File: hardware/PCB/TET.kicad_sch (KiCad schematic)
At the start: 43 parts, among them J1 SWD, M1 MountingHole, M2 MountingHole, M3 MountingHole, M4 MountingHole, U1 TCAN330GDCNR, U2 8 MHz, U3 STM32L431RBT6TR, U4 TMP112AIDRLR

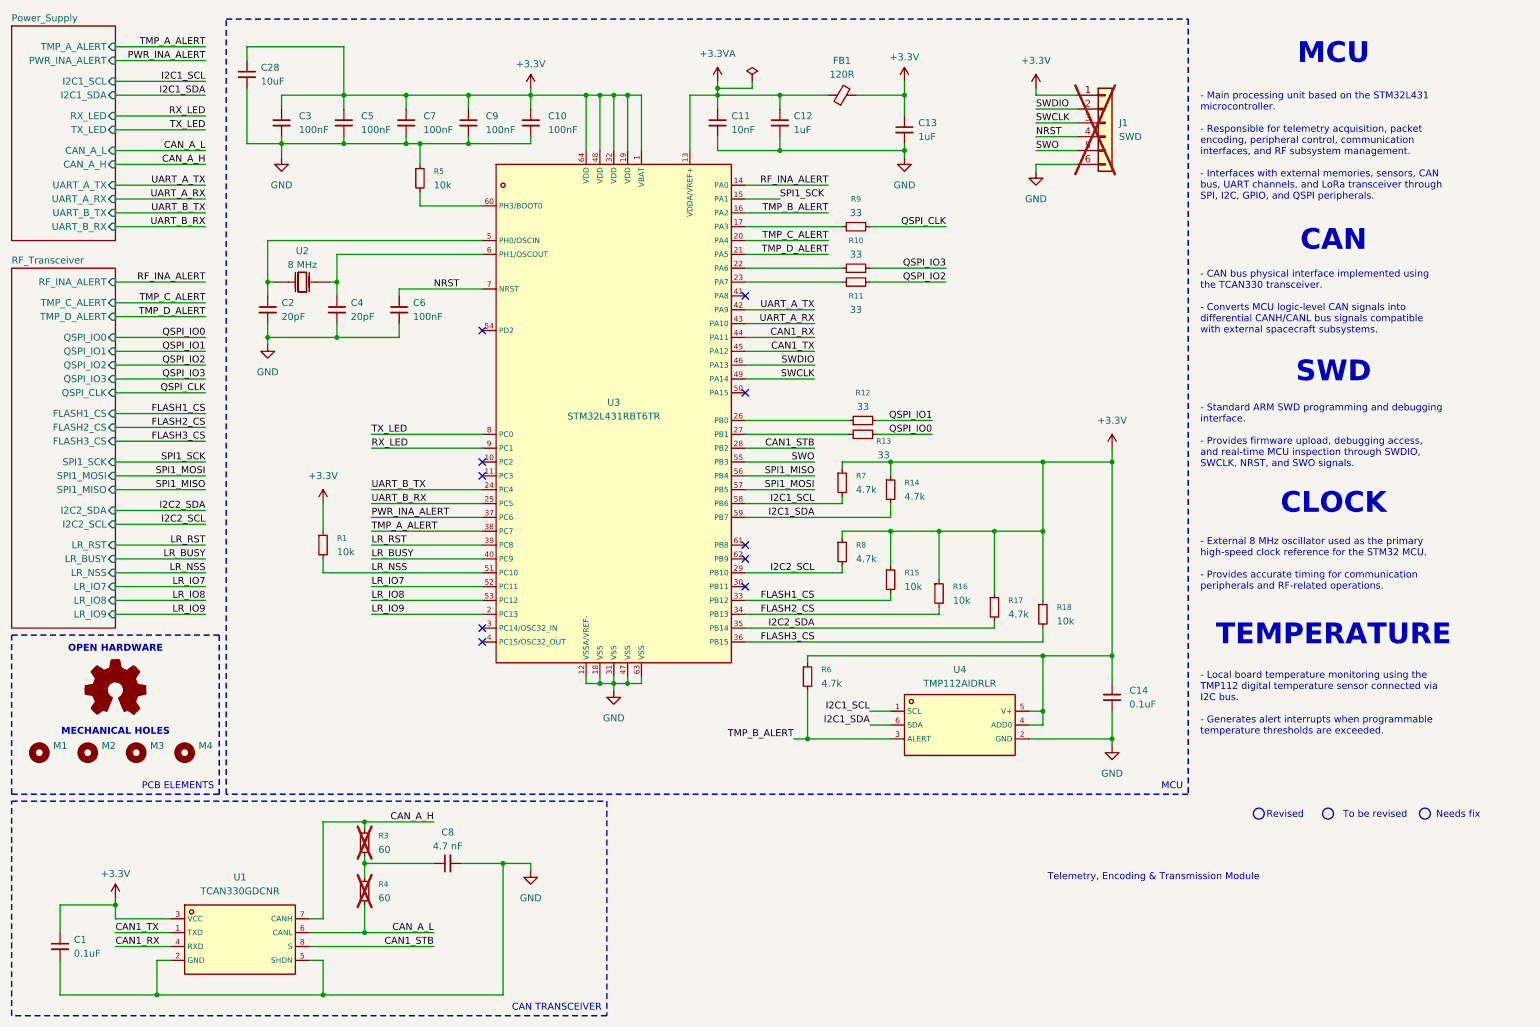
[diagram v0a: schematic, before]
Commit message: feat(hardware): implement TET module PCB design and restructure project
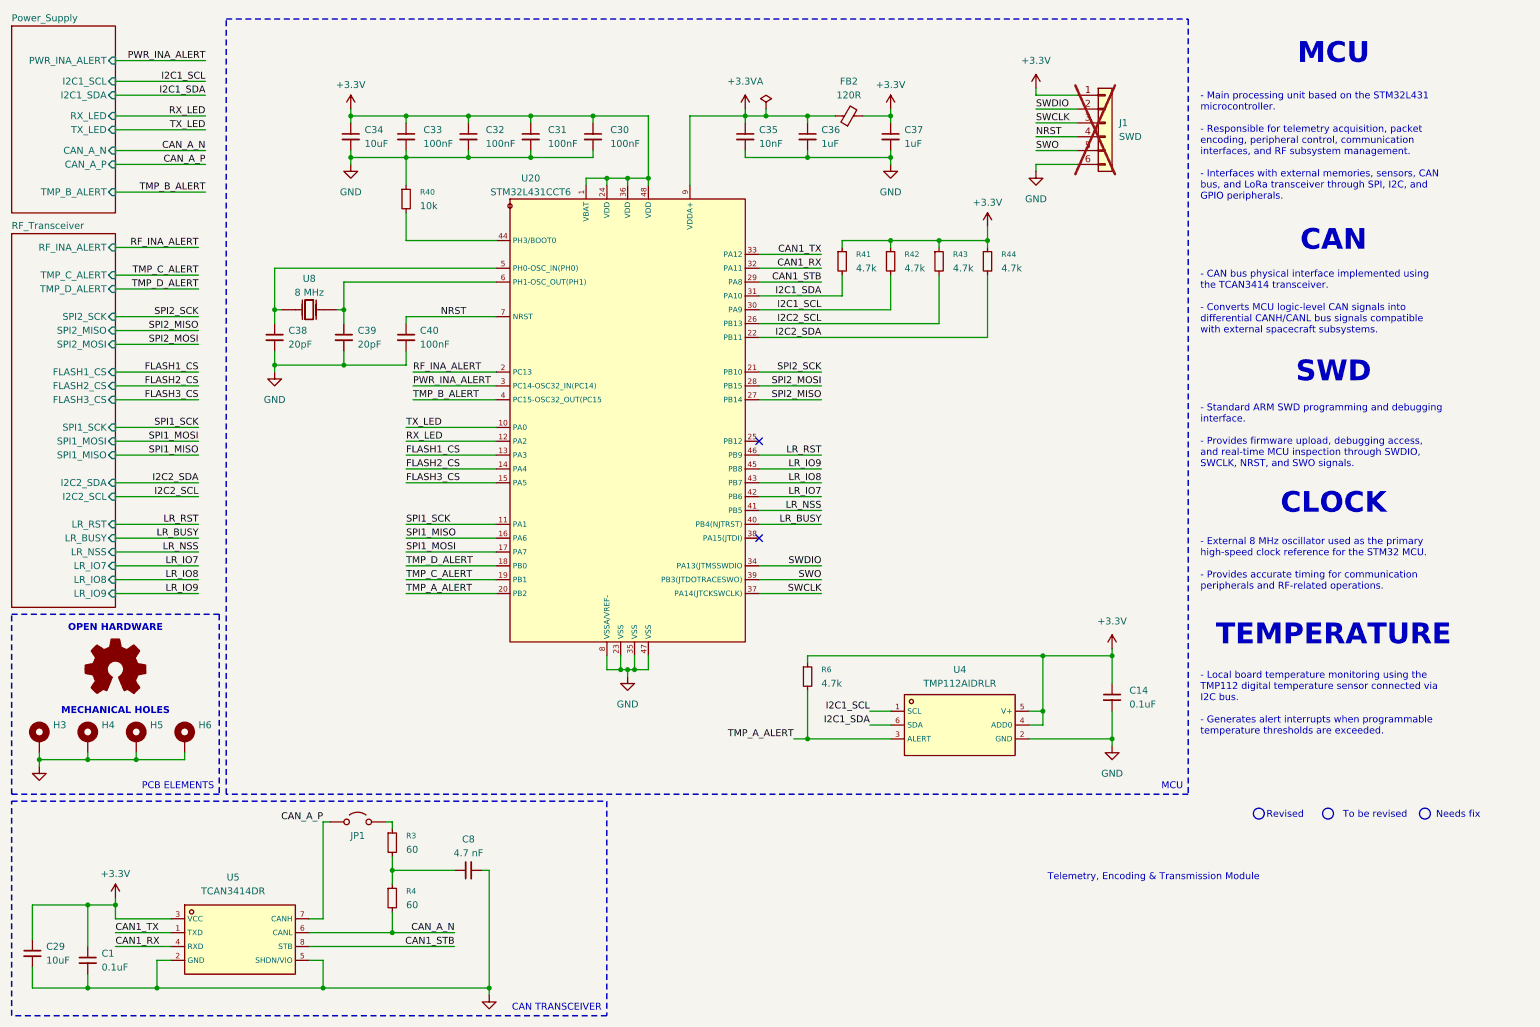
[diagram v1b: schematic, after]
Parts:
- removed C10, C3, C5, C6, C7, C9: 100nF, Capacitor_SMD:C_0603_1608Metric, symbol Device:C_Small
- removed C11: 10nF, Capacitor_SMD:C_0603_1608Metric, symbol Device:C_Small
- removed C12, C13: 1uF, Capacitor_SMD:C_0603_1608Metric, symbol Device:C_Small
- removed C2, C4: 20pF, Capacitor_SMD:C_0603_1608Metric, symbol Device:C_Small
- removed C28: 10uF, Capacitor_SMD:C_0603_1608Metric, symbol Device:C_Small
- removed FB1: 120R, Inductor_SMD:L_0603_1608Metric, symbol Device:FerriteBead_Small
- removed M1, M2, M3, M4: MountingHole, MountingHole:MountingHole_3.2mm_M3_Pad, symbol Mechanical:MountingHole
- removed R1, R15, R16, R18, R5: 10k, Resistor_SMD:R_0603_1608Metric, symbol Device:R_Small
- removed R10, R11, R12, R13, R9: 33, Resistor_SMD:R_0603_1608Metric, symbol Device:R_Small
- removed R14, R17, R7, R8: 4.7k, Resistor_SMD:R_0603_1608Metric, symbol Device:R_Small
- removed U1: TCAN330GDCNR, TET-Footprints:SOT-23-8_L2.9-W1.6-P0.65-LS2.8-BL, symbol TET-Symbols:TCAN330GDCNR
- removed U2: 8 MHz, TET-Footprints:CRYSTAL-SMD_L5.0-W3.2, symbol TET-Symbols:X50328MSB2GI
- removed U3: STM32L431RBT6TR, TET-Footprints:LQFP-64_L10.0-W10.0-P0.50-LS12.0-BL, symbol TET-Symbols:STM32L431RBT6TR
- added C29, C34: 10uF, Capacitor_SMD:C_0402_1005Metric, symbol Device:C_Small
- added C30, C31, C32, C33, C40: 100nF, Capacitor_SMD:C_0402_1005Metric, symbol Device:C_Small
- added C35: 10nF, Capacitor_SMD:C_0402_1005Metric, symbol Device:C_Small
- added C36, C37: 1uF, Capacitor_SMD:C_0402_1005Metric, symbol Device:C_Small
- added C38, C39: 20pF, Capacitor_SMD:C_0402_1005Metric, symbol Device:C_Small
- added FB2: 120R, Inductor_SMD:L_0603_1608Metric, symbol Device:FerriteBead_Small
- added H3, H4, H5, H6: MountingHole_Pad, MountingHole:MountingHole_3.2mm_M3_Pad_Via, symbol Mechanical:MountingHole_Pad
- added JP1: Jumper_2_Open, Jumper:SolderJumper-2_P1.3mm_Open_TrianglePad1.0x1.5mm, symbol Jumper:Jumper_2_Open
- added R40: 10k, Resistor_SMD:R_0402_1005Metric, symbol Device:R_Small
- added R41, R42, R43, R44: 4.7k, Resistor_SMD:R_0402_1005Metric, symbol Device:R_Small
- added U20: STM32L431CCT6, TET-Footprints:LQFP-48_L7.0-W7.0-P0.50-LS9.0-BL, symbol TET-Symbols:STM32L431CCT6
- added U5: TCAN3414DR, TET-Footprints:SOIC-8_L4.9-W3.9-P1.27-LS6.0-BL, symbol TET-Symbols:TCAN3414DR
- added U8: 8 MHz, TET-Footprints:CRYSTAL-SMD_L5.0-W3.2, symbol TET-Symbols:X50328MSB2GI
- C1, C14, C8: footprint Capacitor_SMD:C_0603_1608Metric -> Capacitor_SMD:C_0402_1005Metric
- R3, R4: footprint Resistor_SMD:R_0603_1608Metric_Pad0.98x0.95mm_HandSolder -> Resistor_SMD:R_0402_1005Metric; now fitted
- R6: footprint Resistor_SMD:R_0603_1608Metric -> Resistor_SMD:R_0402_1005Metric
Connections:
- net +3.3V: now also C29.1, C30.1, C31.1, C32.1, C33.1, C34.1, C37.1, FB2.2, R41.1, R42.1, R43.1, R44.1, U20.1 (VBAT), U20.24 (VDD), U20.36 (VDD), U20.48 (VDD), U5.3 (VCC)
- net +3.3VA: now also C35.1, C36.1, FB2.1, U20.9 (VDDA+)
- net CAN1_RX: now also U20.32 (PA11), U5.4 (RXD)
- net CAN1_STB: now also U20.29 (PA8), U5.8 (STB)
- net CAN1_TX: now also U20.33 (PA12), U5.1 (TXD)
- net FLASH1_CS: now also U20.13 (PA3)
- net FLASH2_CS: now also U20.14 (PA4)
- net FLASH3_CS: now also U20.15 (PA5)
- net GND: now also C29.2, C30.2, C31.2, C32.2, C33.2, C34.2, C35.2, C36.2, C37.2, C38.2, C39.2, C40.2, H3.1, H4.1, H5.1, H6.1, R40.1, U20.23 (VSS), U20.35 (VSS), U20.47 (VSS), U20.8 (VSSA/VREF-), U5.2 (GND), U5.5 (SHDN/VIO)
- net I2C1_SCL: now also R42.2, U20.30 (PA9)
- net I2C1_SDA: now also R41.2, U20.31 (PA10)
- net I2C2_SCL: now also R43.2, U20.26 (PB13)
- net I2C2_SDA: now also R44.2, U20.22 (PB11)
- net LR_BUSY: now also U20.40 (PB4(NJTRST))
- net LR_IO7: now also U20.42 (PB6)
- net LR_IO8: now also U20.43 (PB7)
- net LR_IO9: now also U20.45 (PB8)
- net LR_NSS: now also U20.41 (PB5)
- net LR_RST: now also U20.46 (PB9)
- net NRST: now also C40.1, U20.7 (NRST)
- net PWR_INA_ALERT: now also U20.3 (PC14-OSC32_IN(PC14))
- net RF_INA_ALERT: now also U20.2 (PC13)
- net RX_LED: now also U20.12 (PA2)
- net SPI1_MISO: now also U20.16 (PA6)
- net SPI1_MOSI: now also U20.17 (PA7)
- net SPI1_SCK: now also U20.11 (PA1)
- net SWCLK: now also U20.37 (PA14(JTCKSWCLK))
- net SWDIO: now also U20.34 (PA13(JTMSSWDIO)
- net SWO: now also U20.39 (PB3(JTDOTRACESWO))
- net TMP_A_ALERT: now also R6.2, U4.3 (ALERT), U20.20 (PB2)
- net TMP_B_ALERT: now also U20.4 (PC15-OSC32_OUT(PC15); no longer R6.2, U4.3 (ALERT)
- net TMP_C_ALERT: now also U20.19 (PB1)
- net TMP_D_ALERT: now also U20.18 (PB0)
- net TX_LED: now also U20.10 (PA0)
- net CAN_A_H: no longer names the net of R3.1
- net CAN_A_H: now also JP1.2 (B)
- net CAN_A_L renamed CAN_A_N
- net CAN_A_N: now also U5.6 (CANL)
- new net: R40.2, U20.44 (PH3/BOOT0)
- new net: C38.1, U20.5 (PH0-OSC_IN(PH0)), U8.2 (OSC2)
- new net: C39.1, U20.6 (PH1-OSC_OUT(PH1)), U8.1 (OSC1)
- new net CAN_A_P: JP1.1 (A), U5.7 (CANH)
- new net SPI2_MISO: U20.27 (PB14)
- new net SPI2_MOSI: U20.28 (PB15)
- new net SPI2_SCK: U20.21 (PB10)
- no-connect marks 10 -> 2
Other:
- sheet Power_Supply ports: added CAN_A_N, CAN_A_P, TMP_B_ALERT; removed CAN_A_H, CAN_A_L, TMP_A_ALERT, UART_A_RX, UART_A_TX, UART_B_RX, UART_B_TX
- sheet RF_Transceiver ports: added SPI2_MISO, SPI2_MOSI, SPI2_SCK; removed QSPI_CLK, QSPI_IO0, QSPI_IO1, QSPI_IO2, QSPI_IO3
- moved on the sheet: C1, C8

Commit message: feat(hardware): complete PCB layout and project structure
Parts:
- C1, C14: value 0.1uF -> 100nF
- C29, C34: footprint Capacitor_SMD:C_0402_1005Metric -> Capacitor_SMD:C_0805_2012Metric
- J1, JP1: now left out of the parts list
- R3, R4: value 60 -> 60.4
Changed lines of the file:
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@@
 	(title_block
 		(title "TET Module")
-		(date "2026-05-01")
-		(rev "1.0")
+		(date "2026-06-09")
+		(rev "v1r1")
 		(company "ICDT")
-		(comment 1 "PCB-01")
+		(comment 1 "TET-v1r1")
 		(comment 2 "Rodrigo Andrade")
-		(comment 3 "01/05/2026")
+		(comment 3 "09/06/2026")
 	)
